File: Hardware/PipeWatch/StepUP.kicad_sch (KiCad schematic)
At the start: 3 parts

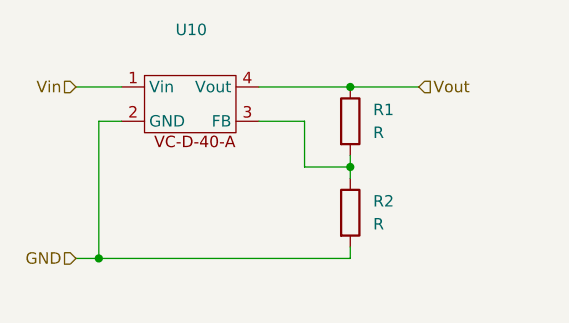
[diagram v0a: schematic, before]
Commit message: Started laying traces
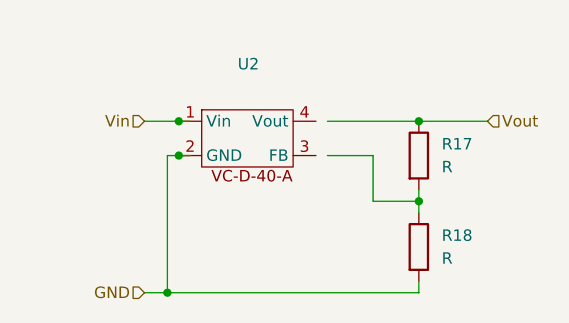
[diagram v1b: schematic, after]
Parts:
- removed R1, R2: R, Resistor_SMD:R_0805_2012Metric_Pad1.20x1.40mm_HandSolder, symbol Device:R
- removed U10: ~, Felix:VC-D-40-A, symbol Felix:VC-D-40-A
- added R17, R18: R, Resistor_SMD:R_0805_2012Metric_Pad1.20x1.40mm_HandSolder, symbol Device:R
- added U2: ~, Felix:VC-D-40-A, symbol Felix:VC-D-40-A
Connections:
- net GND: now also R18.2, U2.2 (GND)
- net Vin: now also U2.1 (Vin)
- net Vout: now also R17.1
- new net: R17.2, R18.1

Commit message: Final Version (Ordered it)
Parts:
- R18: value R -> 680R
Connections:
- net Vout: now also U2.4 (Vout)
- net at U2.3 (FB): now also R17.2, R18.1
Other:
- moved on the sheet: U2
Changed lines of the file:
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@@
-	)
-	(junction
-		(at 125.73 96.52)
-		(diameter 0)
-		(color 0 0 0 0)
 	)
 	(junction
@@
 		(color 0 0 0 0)
 	)
-	(junction
-		(at 125.73 92.71)
-		(diameter 0)
-		(color 0 0 0 0)
-	)
-	(wire
-		(pts
-			(xy 125.73 92.71) (xy 127 92.71)
-		)
-		(stroke
-			(width 0)
-			(type default)
-		)
-	)
 	(wire
 		(pts
@@
 	(wire
 		(pts
-			(xy 121.92 92.71) (xy 125.73 92.71)
+			(xy 121.92 92.71) (xy 127 92.71)
 		)
 		(stroke
@@
 	(wire
 		(pts
-			(xy 125.73 96.52) (xy 127 96.52)
-		)
-		(stroke
-			(width 0)
-			(type default)
-		)
-	)
-	(wire
-		(pts
 			(xy 152.4 101.6) (xy 152.4 100.33)
 		)
@@
 	(wire
 		(pts
-			(xy 124.46 96.52) (xy 125.73 96.52)
+			(xy 124.46 96.52) (xy 127 96.52)
 		)
 		(stroke
@@
 	(symbol
 		(lib_id "Felix:VC-D-40-A")
-		(at 128.27 97.79 0)
+		(at 129.54 97.79 0)
 		(unit 1)
 		(exclude_from_sim no)
@@
 		(fields_autoplaced yes)
 		(property "Reference" "U2"
-			(at 133.462 86.36 0)
+			(at 134.732 86.36 0)
 			(effects
 				(font
@@
 		)
 		(property "Value" "~"
-			(at 133.462 88.9 0)
+			(at 134.732 88.9 0)
 			(effects
 				(font
@@
 		)
 		(property "Footprint" "Felix:VC-D-40-A"
-			(at 128.27 97.79 0)
+			(at 129.54 97.79 0)
 			(effects
 				(font
@@
 		)
 		(property "Datasheet" ""
-			(at 128.27 97.79 0)
+			(at 129.54 97.79 0)
 			(effects
 				(font
@@
 		)
 		(property "Description" ""
-			(at 128.27 97.79 0)
+			(at 129.54 97.79 0)
 			(effects
 				(font
@@
 		(fields_autoplaced yes)
 		(property "Reference" "R18"
-			(at 154.94 105.4099 0)
+			(at 154.94 105.41 0)
 			(effects
 				(font
@@
 			)
 		)
-		(property "Value" "R"
-			(at 154.94 107.9499 0)
-			(effects
-				(font
+		(property "Value" "680R"
+			(at 154.94 107.95 0)
+			(effects
+				(font

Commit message: Changed the scematic page Labeling
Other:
- company: (none) -> Felix Pelster
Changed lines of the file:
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@@
 	(generator_version "9.0")
 	(paper "A4")
+	(title_block
+		(date "2025-09-24")
+		(company "Felix Pelster")
+	)
 	(junction
 		(at 152.4 92.71)
